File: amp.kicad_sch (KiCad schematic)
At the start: 32 parts, among them J10 JST_SH_1x4_SM04B-SRSS-TB-LF-SN, J12 JST_XH_1x2_S2B-XH-A-LF-SN, J5 Phone_TRS_MiniJack_SJ-3523-SM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, J9 JST_SUR_1x5_BM05B-SURS-TB-LF-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, U3 TAS2505IRGER, Y2 Oscillator_50MHz_ECS_1612MV

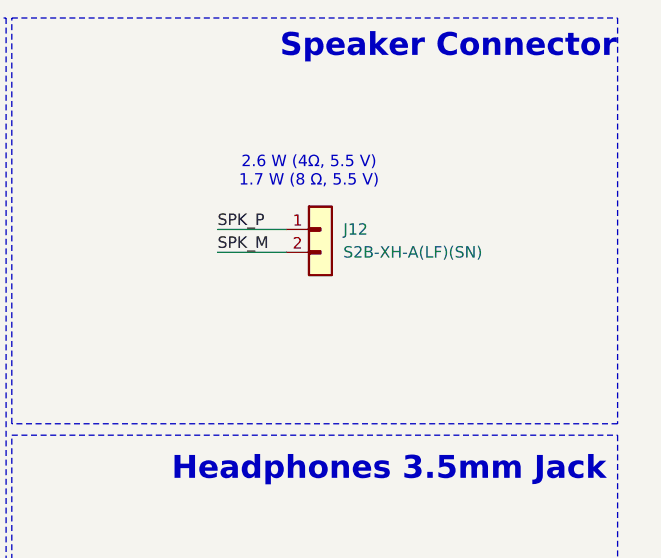
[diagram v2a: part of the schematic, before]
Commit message: [#71555] Update components, start placement
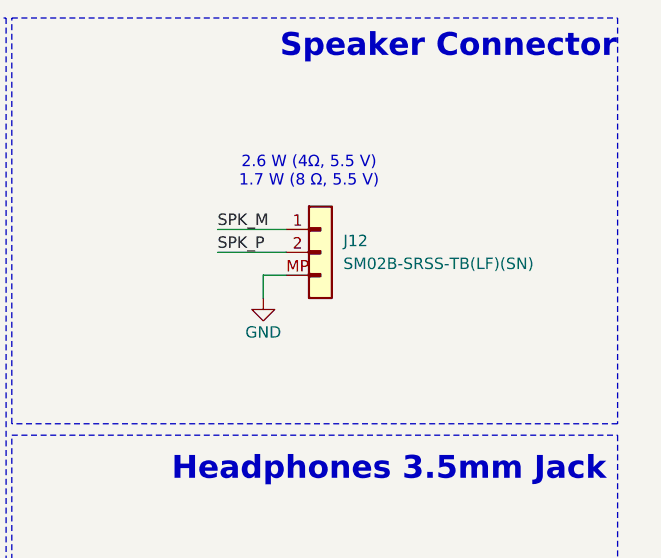
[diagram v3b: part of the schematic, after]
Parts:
- removed J12: JST_XH_1x2_S2B-XH-A-LF-SN, antmicro-footprints:Conn_JST_XH_1x2_S2B-XH-A-LF-SN, symbol antmicroWire2BoardConnectors:JST_XH_1x2_S2B-XH-A-LF-SN
- added J12: JST_SH_1x2_SM02B-SRSS-TB-LF-SN, antmicro-footprints:Conn_JST_SH_1x2_SM02B-SRSS-TB-LF-SN, symbol antmicroWire2BoardConnectors:JST_SH_1x2_SM02B-SRSS-TB-LF-SN
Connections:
- net GND: now also J12.MP
- net SPK_M: now also J12.1
- net SPK_P: now also J12.2
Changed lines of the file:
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@@
 	(wire
 		(pts
+			(xy 293.37 100.33) (xy 295.91 100.33)
+		)
+		(stroke
+			(width 0)
+			(type default)
+		)
+	)
+	(wire
+		(pts
 			(xy 213.36 128.27) (xy 224.79 128.27)
 		)
@@
 	(wire
 		(pts
-			(xy 288.29 97.79) (xy 295.91 97.79)
+			(xy 288.29 95.25) (xy 295.91 95.25)
 		)
 		(stroke
@@
 	(wire
 		(pts
+			(xy 293.37 102.87) (xy 293.37 100.33)
+		)
+		(stroke
+			(width 0)
+			(type default)
+		)
+	)
+	(wire
+		(pts
 			(xy 217.17 207.01) (xy 237.49 207.01)
 		)
@@
 	(wire
 		(pts
-			(xy 288.29 95.25) (xy 295.91 95.25)
+			(xy 288.29 97.79) (xy 295.91 97.79)
 		)
 		(stroke
@@
 	)
 	(label "SPK_P"
-		(at 288.29 95.25 0)
+		(at 288.29 97.79 0)
 		(fields_autoplaced yes)
 		(effects
@@
 	)
 	(label "SPK_M"
-		(at 288.29 97.79 0)
+		(at 288.29 95.25 0)
 		(fields_autoplaced yes)
 		(effects
@@
 	)
 	(symbol
+		(lib_id "antmicroWire2BoardConnectors:JST_SH_1x2_SM02B-SRSS-TB-LF-SN")
+		(at 295.91 95.25 0)
+		(unit 1)
+		(exclude_from_sim no)
+		(in_bom yes)
+		(on_board yes)
+		(dnp no)
+		(fields_autoplaced yes)
+		(property "Reference" "J12"
+			(at 302.26 96.52 0)
+			(effects
+				(font
+					(size 1.27 1.27)
+					(thickness 0.15)
+				)
+				(justify left)
+			)
+		)
+		(property "Value" "JST_SH_1x2_SM02B-SRSS-TB-LF-SN"
+			(at 322.58 101.6 0)
+			(effects
+				(font
+					(size 1.27 1.27)
+					(thickness 0.15)
+				)
+				(justify left bottom)
+				(hide yes)
+			)
+		)
+		(property "Footprint" "antmicro-footprints:Conn_JST_SH_1x2_SM02B-SRSS-TB-LF-SN"
+			(at 322.58 104.14 0)
+			(effects
+				(font
+					(size 1.27 1.27)
+					(thickness 0.15)
+				)
+				(justify left bottom)
+				(hide yes)
+			)
+		)
+		(property "Datasheet" "https://www.jst-mfg.com/product/pdf/eng/eSH.pdf"
+			(at 322.58 106.68 0)
+			(effects
+				(font
+					(size 1.27 1.27)
+					(thickness 0.15)
+				)
+				(justify left bottom)
+				(hide yes)
+			)
+		)
+		(property "Description" "Rectangular connector, header"
+			(at 295.91 95.25 0)
+			(effects
+				(font
+					(size 1.27 1.27)
+				)
+				(hide yes)
+			)
+		)
+		(property "MPN" "SM02B-SRSS-TB(LF)(SN)"
+			(at 302.26 99.06 0)
+			(effects
+				(font
+					(size 1.27 1.27)
+					(thickness 0.15)
+				)
+				(justify left)
+			)
+		)
+		(property "Manufacturer" "JST Automotive Connectors"
+			(at 322.58 111.76 0)
+			(effects
+				(font
+					(size 1.27 1.27)
+					(thickness 0.15)
+				)
+				(justify left bottom)
+				(hide yes)
+			)
+		)
+		(property "Author" "Antmicro"
+			(at 322.58 114.3 0)
+			(effects
+				(font
+					(size 1.27 1.27)
+					(thickness 0.15)
+				)
+				(justify left bottom)
+				(hide yes)
+			)
+		)
+		(property "License" "Apache-2.0"
+			(at 322.58 116.84 0)
+			(effects
+				(font
+					(size 1.27 1.27)
+					(thickness 0.15)
+				)
+				(justify left bottom)
+				(hide yes)
+			)
+		)
+		(pin "1"
+		)
+		(pin "2"
+		)
+		(pin "MP"
+		)
+		(instances
+			(project ""
+				(path "/7fb12ebf-f685-4412-b638-445b1bf344bc/80300fa7-dce3-4149-8e27-6609cbfb608d"
+					(reference "J12")
+					(unit 1)
+				)
+			)
+		)
+	)
+	(symbol
 		(lib_id "antmicropower:GND")
 		(at 214.63 160.02 0)
@@
 	)
 	(symbol
+		(lib_id "antmicropower:GND")
+		(at 293.37 102.87 0)
+		(unit 1)
+		(exclude_from_sim no)
+		(in_bom yes)
+		(on_board yes)
+		(dnp no)
+		(property "Reference" "#PWR0160"
+			(at 302.26 105.41 0)
+			(effects
+				(font
+					(size 1.27 1.27)
+					(thickness 0.15)
+				)
+				(justify left bottom)
+				(hide yes)
+			)
+		)
+		(property "Value" "GND"
+			(at 293.37 106.68 0)
+			(effects
+				(font
+					(size 1.27 1.27)
+					(thickness 0.15)
+				)
+			)
+		)
+		(property "Footprint" ""
+			(at 302.26 110.49 0)
+			(effects
+				(font
+					(size 1.27 1.27)
+					(thickness 0.15)
+				)
+				(justify left bottom)
+				(hide yes)
+			)
+		)
+		(property "Datasheet" ""
+			(at 302.26 115.57 0)
+			(effects
+				(font
+					(size 1.27 1.27)
+					(thickness 0.15)
+				)
+				(justify left bottom)
+				(hide yes)
+			)
+		)
+		(property "Description" ""
+			(at 293.37 102.87 0)
+			(effects
+				(font
+					(size 1.27 1.27)
+				)
+				(hide yes)
+			)
+		)
+		(property "Author" "Antmicro"
+			(at 302.26 110.49 0)
+			(effects
+				(font
+					(size 1.27 1.27)
+					(thickness 0.15)
+				)
+				(justify left bottom)
+				(hide yes)
+			)
+		)
+		(property "License" "Apache-2.0"
+			(at 302.26 113.03 0)
+			(effects
+				(font
+					(size 1.27 1.27)
+					(thickness 0.15)
+				)
+				(justify left bottom)
+				(hide yes)
+			)
+		)
+		(pin "1"
+		)
+		(instances
+			(project "audio-latency-processing-board"
+				(path "/7fb12ebf-f685-4412-b638-445b1bf344bc/80300fa7-dce3-4149-8e27-6609cbfb608d"
+					(reference "#PWR0160")
+					(unit 1)
+				)
+			)
+		)
+	)
+	(symbol
 		(lib_id "antmicropower:+1V8")
 		(at 134.62 85.09 0)
@@
 					(unit 1)
 				)
-			)
-		)
-	)
-	(symbol
-		(lib_id "antmicroWire2BoardConnectors:JST_XH_1x2_S2B-XH-A-LF-SN")
-		(at 295.91 95.25 0)
-		(unit 1)
-		(exclude_from_sim no)
-		(in_bom yes)
-		(on_board yes)
-		(dnp no)
-		(fields_autoplaced yes)
-		(property "Reference" "J12"
-			(at 302.26 95.25 0)
-			(effects
-				(font
-					(size 1.27 1.27)
-					(thickness 0.15)
-				)
-				(justify left)
-			)
-		)
-		(property "Value" "JST_XH_1x2_S2B-XH-A-LF-SN"
-			(at 321.31 105.41 0)
-			(effects
-				(font
-					(size 1.27 1.27)
-					(thickness 0.15)
-				)
-				(justify left bottom)
-				(hide yes)
-			)
-		)
-		(property "Footprint" "antmicro-footprints:Conn_JST_XH_1x2_S2B-XH-A-LF-SN"
-			(at 321.31 107.95 0)
-			(effects
-				(font
-					(size 1.27 1.27)
-					(thickness 0.15)
-				)
-				(justify left bottom)
-				(hide yes)
-			)
-		)
-		(property "Datasheet" "https://www.tme.eu/Document/0a99312bb6c67d3f0f7869fe9a023cea/XH.pdf"
-			(at 321.31 110.49 0)
-			(effects
-				(font
-					(size 1.27 1.27)
-					(thickness 0.15)
-				)
-				(justify left bottom)
-				(hide yes)
-			)
-		)
-		(property "Description" "Connector Header Through Hole, Right Angle 2 position 0.098\" (2.50mm)"
-			(at 295.91 95.25 0)
-			(effects
-				(font
-					(size 1.27 1.27)
-				)
-				(hide yes)
-			)
-		)
-		(property "MPN" "S2B-XH-A(LF)(SN)"
-			(at 302.26 97.79 0)
-			(effects
-				(font
-					(size 1.27 1.27)
-					(thickness 0.15)
-				)
-				(justify left)
-			)
-		)
-		(property "Manufacturer" "JST Automotive Connectors"
-			(at 321.31 102.87 0)
-			(effects
-				(font
-					(size 1.27 1.27)
-					(thickness 0.15)
-				)
-				(justify left bottom)
-				(hide yes)
-			)
-		)
-		(property "Author" "Antmicro"
-			(at 321.31 113.03 0)
-			(effects
-				(font
-					(size 1.27 1.27)
-					(thickness 0.15)
-				)
-				(justify left bottom)
-				(hide yes)
-			)
-		)
-		(property "License" "Apache-2.0"
-			(at 321.31 115.57 0)
-			(effects
-				(font
-					(size 1.27 1.27)
-					(thickness 0.15)
-				)
-				(justify left bottom)
-				(hide yes)
-			)
-		)
-		(pin "2"
-		)
-		(pin "1"
-		)
-		(instances
-			(project ""
-				(path "/7fb12ebf-f685-4412-b638-445b1bf344bc/80300fa7-dce3-4149-8e27-6609cbfb608d"
-					(reference "J12")
-					(unit 1)
-				)
